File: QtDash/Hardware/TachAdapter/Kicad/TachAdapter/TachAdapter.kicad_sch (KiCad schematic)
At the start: 13 parts, among them J1 In, J2 Out, U1 H11L1

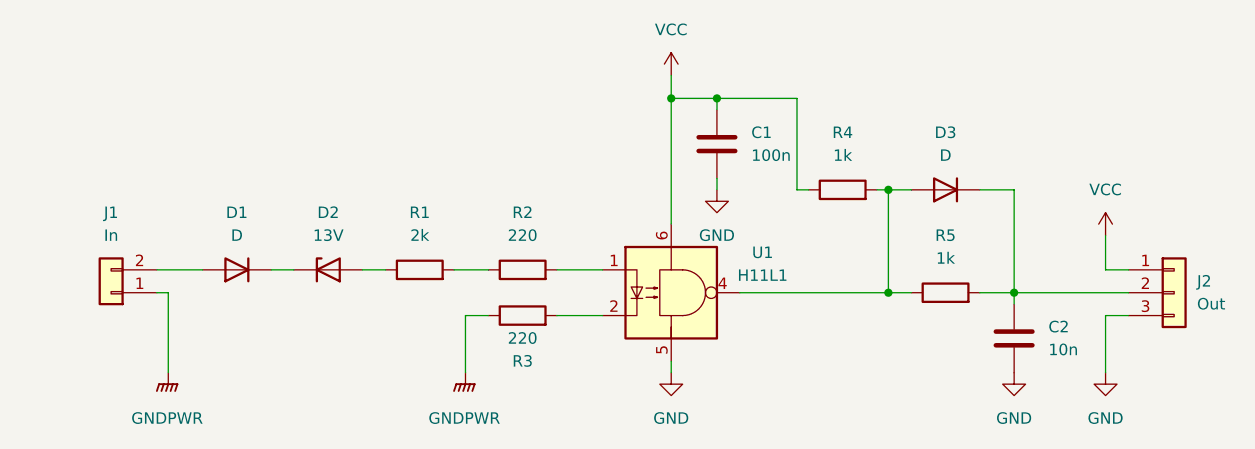
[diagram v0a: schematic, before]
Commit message: topic/documentation-update: 	- added tach adapter revision documentation for kicad and eagle
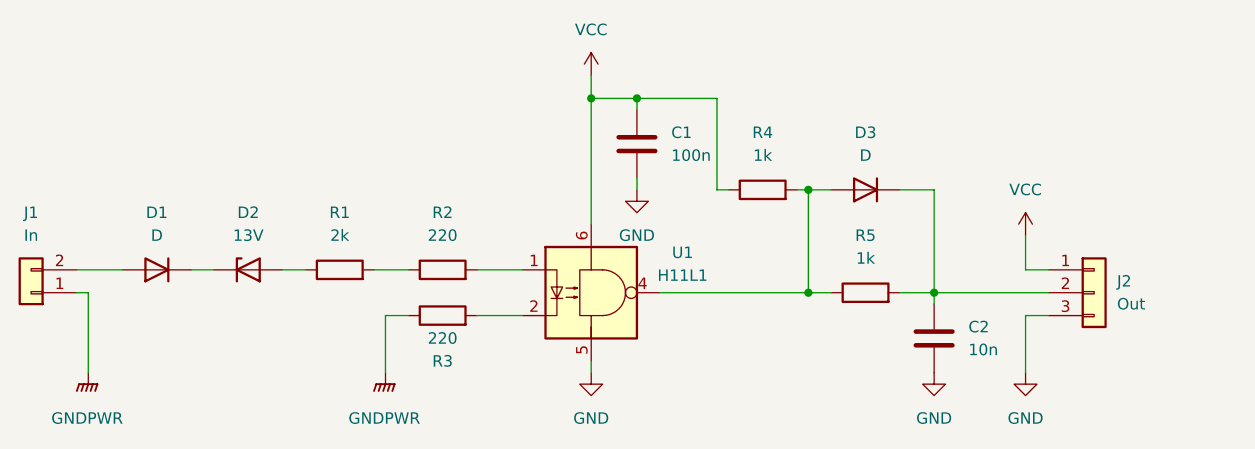
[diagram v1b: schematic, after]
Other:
- title: (none) -> Volvo 240 Digital Dash Tach Adapter
- moved on the sheet: C1, C2, D1, D2, D3, J1, J2, R1, R2, R3, R4, R5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

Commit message: 82-bom-missing: 	- added BOM for kicad version of tach adapter
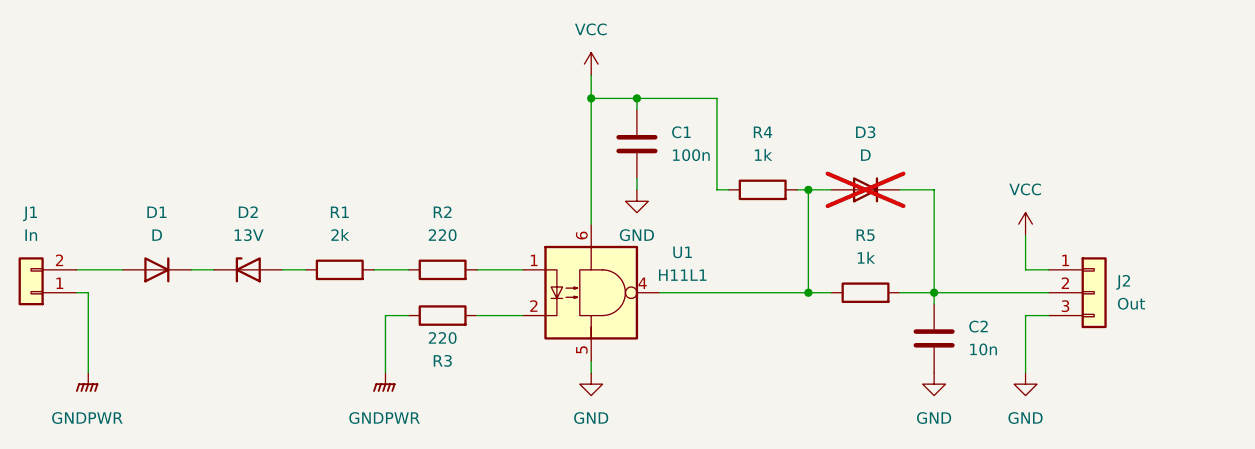
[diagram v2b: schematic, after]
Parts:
- C1: PN (none) -> CL10B104MB8NNNC
- C2: PN (none) -> CL10B103KB8NNNC
- D1: PN (none) -> RS2GA-13-F
- D2: PN (none) -> CZRB5350B-HF
- D3: PN (none) -> RS2GA-13-F; now not fitted
- R1: PN (none) -> CRCW12062K00JNEAHP
- R2, R3: PN (none) -> CRCW1206220RFKEAHP
- R4, R5: PN (none) -> RC0603JR-071KL
- U1: PN (none) -> H11L1

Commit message: 82-bom-missing: 	- it helps if you add part numbers
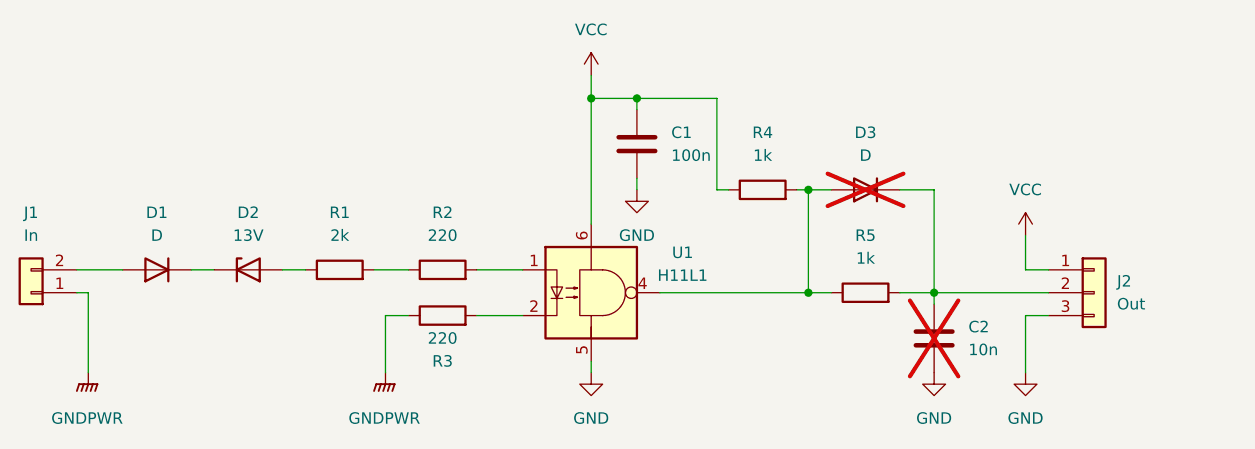
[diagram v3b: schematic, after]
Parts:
- C2: now not fitted
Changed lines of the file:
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@@
 		(in_bom yes)
 		(on_board yes)
-		(dnp no)
+		(dnp yes)
 		(fields_autoplaced yes)
 		(property "Reference" "C2"
